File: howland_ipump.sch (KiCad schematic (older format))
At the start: 13 parts, among them Q1 BC856, U11 OPA991S

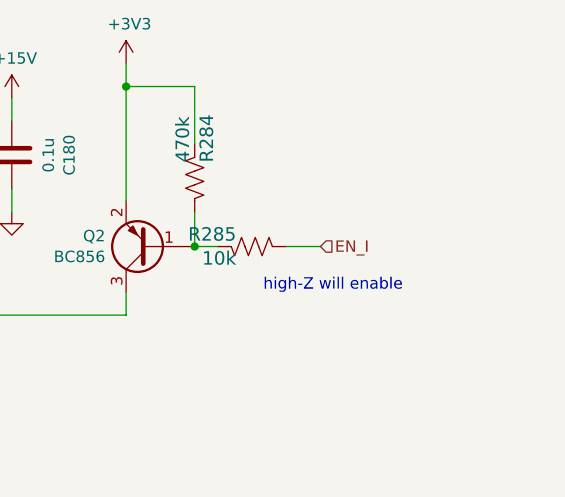
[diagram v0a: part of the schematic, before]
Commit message: layout cleanup; removed custom footrpints
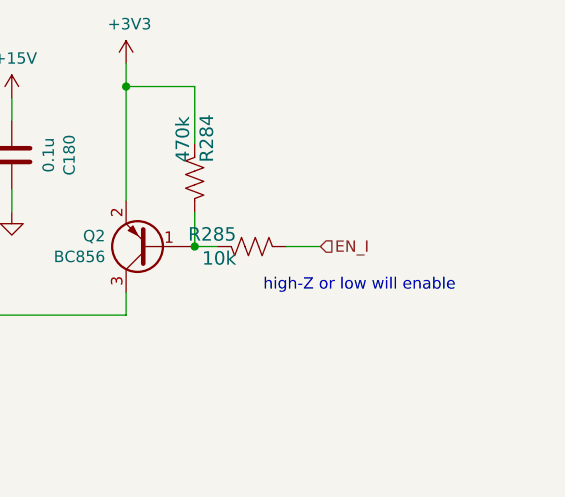
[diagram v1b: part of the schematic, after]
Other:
- note added: "high-Z or low will enable"
- note removed: "high-Z will enable"
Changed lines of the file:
@@
 EN_I
 Text Notes 8250 4250 0    50   ~ 0
-high-Z will enable
+high-Z or low will enable
 Wire Wire Line
 	5100 4000 5100 4050

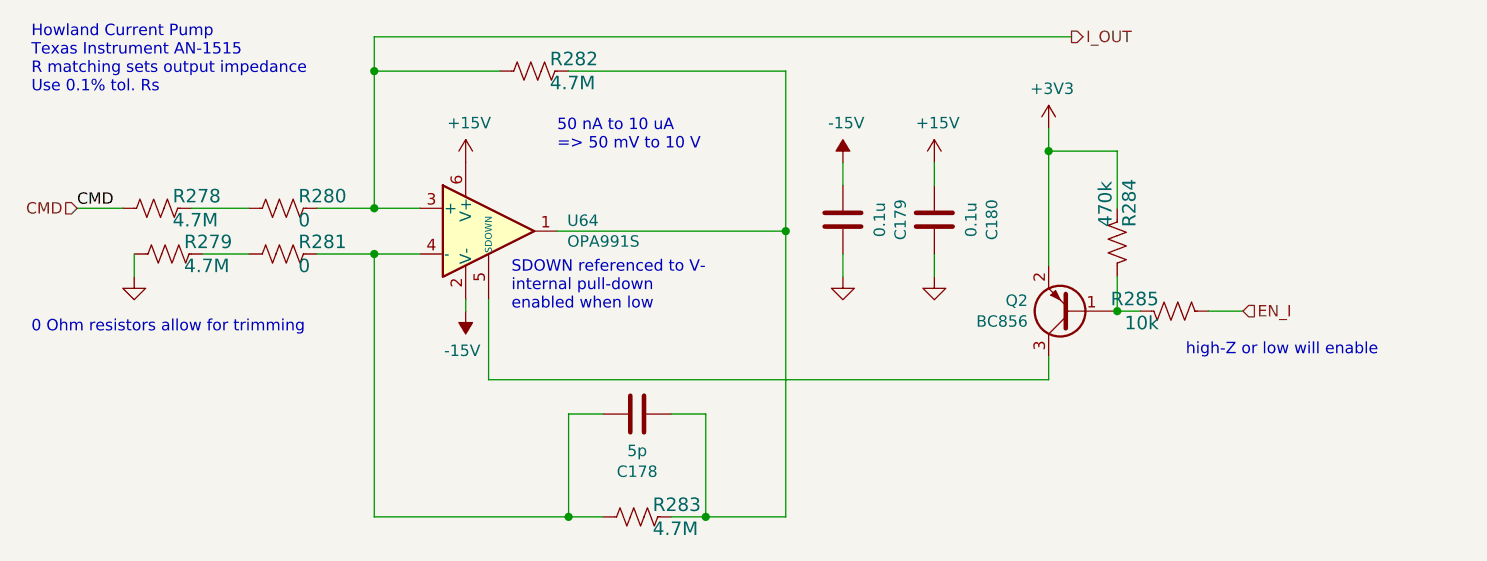
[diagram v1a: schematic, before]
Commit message: updates of DAC part placement
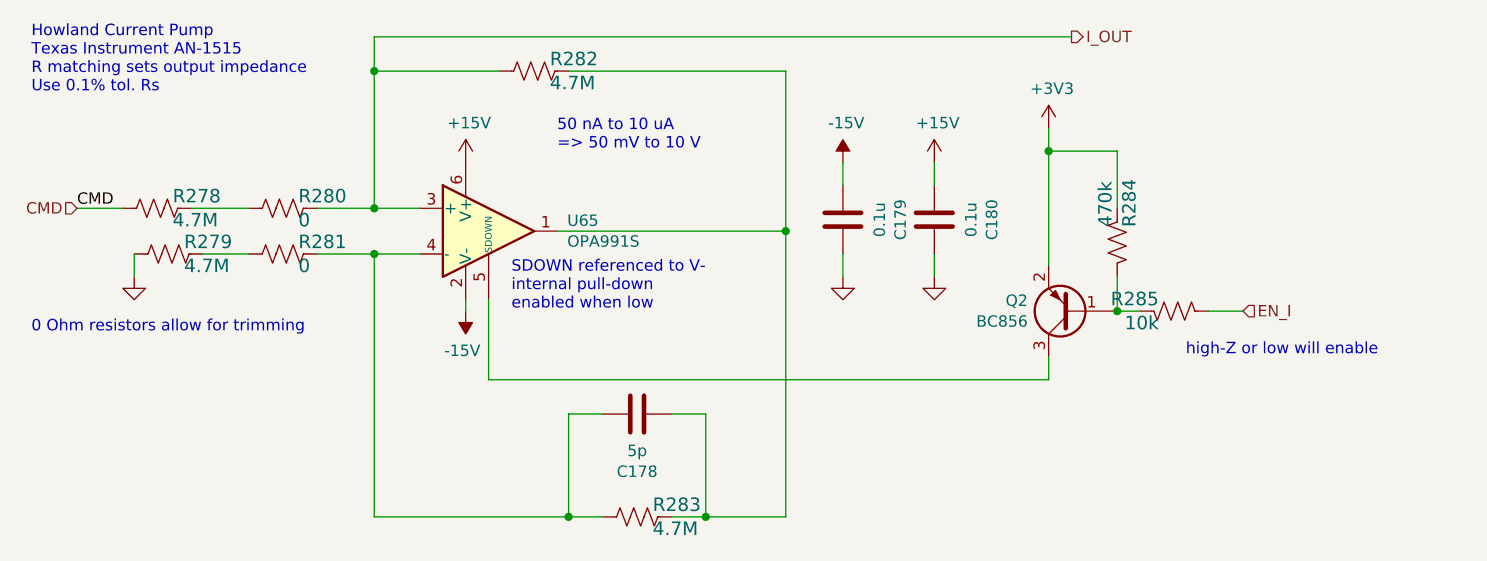
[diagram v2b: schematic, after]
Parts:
- renumbered C33 to C11, C34 to C12, C35 to C13, R28 to R27, R52 to R28, R53 to R29, R54 to R30, R59 to R31, R60 to R32, R26 to R33, R27 to R34, U11 to U12

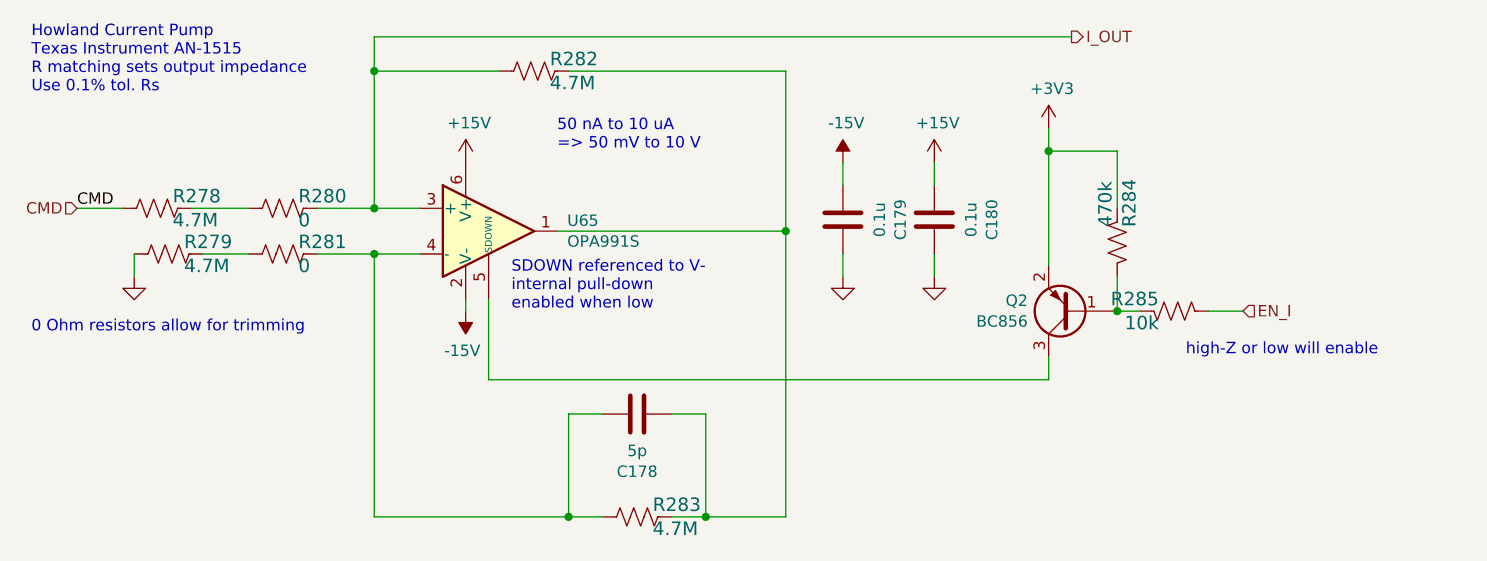
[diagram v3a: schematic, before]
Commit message: updated component placement
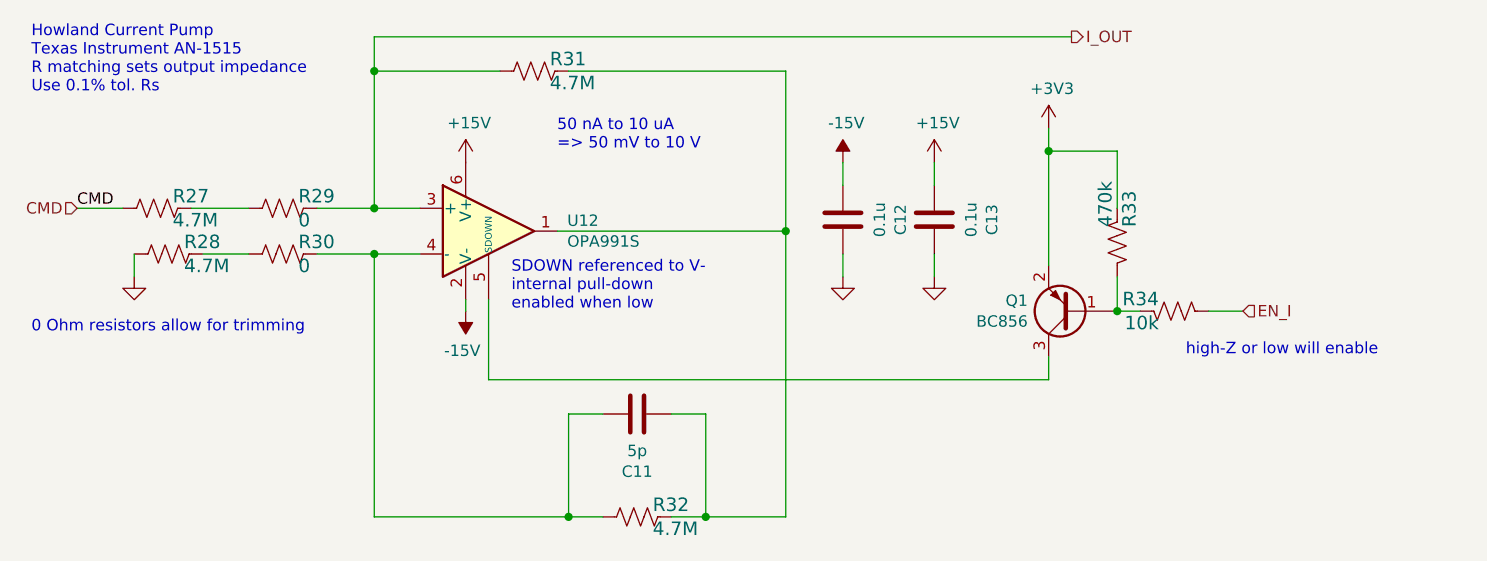
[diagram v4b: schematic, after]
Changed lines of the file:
@@
 AR Path="/6095BD4C/60C5A41E/60D781E3" Ref="#PWR?"  Part="1"
 AR Path="/61B02572/60BE01FC/60D781E3" Ref="#PWR0254"  Part="1"
-F 0 "#PWR0254" H 5100 4150 50  0001 C CNN
+F 0 "#PWR059" H 5100 4150 50  0001 C CNN
 F 1 "-15V" H 5115 4223 50  0000 C CNN
 F 2 "" H 5100 4050 50  0001 C CNN
@@
 AR Path="/6095BD4C/60C5A41E/60D781E9" Ref="#PWR?"  Part="1"
 AR Path="/61B02572/60BE01FC/60D781E9" Ref="#PWR0253"  Part="1"
-F 0 "#PWR0253" H 5100 3250 50  0001 C CNN
+F 0 "#PWR058" H 5100 3250 50  0001 C CNN
 F 1 "+15V" H 5115 3573 50  0000 C CNN
 F 2 "" H 5100 3400 50  0001 C CNN
@@
 AR Path="/6095BD4C/60C5A41E/60D781F4" Ref="C?"  Part="1"
 AR Path="/61B02572/60BE01FC/60D781F4" Ref="C178"  Part="1"
-F 0 "C178" V 5598 4500 50  0000 C CNN
+F 0 "C11" V 5598 4500 50  0000 C CNN
 F 1 "5p" V 5689 4500 50  0000 C CNN
 F 2 "Capacitor_SMD:C_0603_1608Metric" H 5888 4350 50  0001 C CNN
@@
 AR Path="/6095BD4C/60C5A41E/60D78215" Ref="#PWR?"  Part="1"
 AR Path="/61B02572/60BE01FC/60D78215" Ref="#PWR0252"  Part="1"
-F 0 "#PWR0252" H 3650 3650 50  0001 C CNN
+F 0 "#PWR057" H 3650 3650 50  0001 C CNN
 F 1 "GND" V 3655 3772 50  0001 R CNN
 F 2 "" H 3650 3900 50  0001 C CNN
@@
 AR Path="/6095BD4C/60C5A41E/60D7821F" Ref="U?"  Part="1"
 AR Path="/61B02572/60BE01FC/60D7821F" Ref="U65"  Part="1"
-F 0 "U65" H 5544 3746 50  0000 L CNN
+F 0 "U12" H 5544 3746 50  0000 L CNN
 F 1 "OPA991S" H 5544 3655 50  0000 L CNN
 F 2 "Package_TO_SOT_SMD:SOT-23-6" H 5350 3450 50  0001 L CNN
@@
 AR Path="/6095BD4C/60C5A41E/60D78240" Ref="R?"  Part="1"
 AR Path="/61B02572/60BE01FC/60D78240" Ref="R283"  Part="1"
-F 0 "R283" V 5797 5018 59  0000 L CNN
+F 0 "R32" V 5797 5018 59  0000 L CNN
 F 1 "4.7M" V 5902 5018 59  0000 L CNN
 F 2 "Resistor_SMD:R_1206_3216Metric" H 5850 4950 50  0001 C CNN
@@
 AR Path="/6095BD4C/60C5A41E/60D7824A" Ref="C?"  Part="1"
 AR Path="/61B02572/60BE01FC/60D7824A" Ref="C179"  Part="1"
-F 0 "C179" V 6498 3650 50  0000 C CNN
+F 0 "C12" V 6498 3650 50  0000 C CNN
 F 1 "0.1u" V 6589 3650 50  0000 C CNN
 F 2 "Capacitor_SMD:C_0603_1608Metric" H 6788 3500 50  0001 C CNN
@@
 AR Path="/6095BD4C/60C5A41E/60D78250" Ref="#PWR?"  Part="1"
 AR Path="/61B02572/60BE01FC/60D78250" Ref="#PWR0256"  Part="1"
-F 0 "#PWR0256" H 6750 3650 50  0001 C CNN
+F 0 "#PWR061" H 6750 3650 50  0001 C CNN
 F 1 "GND" V 6755 3772 50  0001 R CNN
 F 2 "" H 6750 3900 50  0001 C CNN
@@
 AR Path="/6095BD4C/60C5A41E/60D78256" Ref="#PWR?"  Part="1"
 AR Path="/61B02572/60BE01FC/60D78256" Ref="#PWR0257"  Part="1"
-F 0 "#PWR0257" H 7150 3250 50  0001 C CNN
+F 0 "#PWR062" H 7150 3250 50  0001 C CNN
 F 1 "+15V" H 7165 3573 50  0000 C CNN
 F 2 "" H 7150 3400 50  0001 C CNN
@@
 AR Path="/6095BD4C/60C5A41E/60D7825C" Ref="#PWR?"  Part="1"
 AR Path="/61B02572/60BE01FC/60D7825C" Ref="#PWR0258"  Part="1"
-F 0 "#PWR0258" H 7150 3650 50  0001 C CNN
+F 0 "#PWR063" H 7150 3650 50  0001 C CNN
 F 1 "GND" V 7155 3772 50  0001 R CNN
 F 2 "" H 7150 3900 50  0001 C CNN
@@
 AR Path="/6095BD4C/60C5A41E/60D78264" Ref="C?"  Part="1"
 AR Path="/61B02572/60BE01FC/60D78264" Ref="C180"  Part="1"
-F 0 "C180" V 6898 3650 50  0000 C CNN
+F 0 "C13" V 6898 3650 50  0000 C CNN
 F 1 "0.1u" V 6989 3650 50  0000 C CNN
 F 2 "Capacitor_SMD:C_0603_1608Metric" H 7188 3500 50  0001 C CNN
@@
 AR Path="/6095BD4C/60C5A41E/60D7826A" Ref="#PWR?"  Part="1"
 AR Path="/61B02572/60BE01FC/60D7826A" Ref="#PWR0255"  Part="1"
-F 0 "#PWR0255" H 6750 3500 50  0001 C CNN
+F 0 "#PWR060" H 6750 3500 50  0001 C CNN
 F 1 "-15V" H 6765 3573 50  0000 C CNN
 F 2 "" H 6750 3400 50  0001 C CNN
@@
 AR Path="/6095BD4C/60C5A41E/60D83006" Ref="R?"  Part="1"
 AR Path="/61B02572/60BE01FC/60D83006" Ref="R281"  Part="1"
-F 0 "R281" V 4247 3868 59  0000 L CNN
+F 0 "R30" V 4247 3868 59  0000 L CNN
 F 1 "0" V 4352 3868 59  0000 L CNN
 F 2 "Resistor_SMD:R_0603_1608Metric" H 4300 3800 50  0001 C CNN
@@
 AR Path="/6095BD4C/60C5A41E/60D8879F" Ref="R?"  Part="1"
 AR Path="/61B02572/60BE01FC/60D8879F" Ref="R280"  Part="1"
-F 0 "R280" V 4247 3668 59  0000 L CNN
+F 0 "R29" V 4247 3668 59  0000 L CNN
 F 1 "0" V 4352 3668 59  0000 L CNN
 F 2 "Resistor_SMD:R_0603_1608Metric" H 4300 3600 50  0001 C CNN
@@
 AR Path="/6095BD4C/60C5A41E/60B385AE" Ref="R?"  Part="1"
 AR Path="/61B02572/60BE01FC/60B385AE" Ref="R279"  Part="1"
-F 0 "R279" V 3747 3868 59  0000 L CNN
+F 0 "R28" V 3747 3868 59  0000 L CNN
 F 1 "4.7M" V 3852 3868 59  0000 L CNN
 F 2 "Resistor_SMD:R_1206_3216Metric" H 3800 3800 50  0001 C CNN
@@
 AR Path="/6095BD4C/60C5A41E/60B38EA4" Ref="R?"  Part="1"
 AR Path="/61B02572/60BE01FC/60B38EA4" Ref="R278"  Part="1"
-F 0 "R278" V 3697 3668 59  0000 L CNN
+F 0 "R27" V 3697 3668 59  0000 L CNN
 F 1 "4.7M" V 3802 3668 59  0000 L CNN
 F 2 "Resistor_SMD:R_1206_3216Metric" H 3750 3600 50  0001 C CNN
@@
 AR Path="/6095BD4C/60C5A41E/60B3940D" Ref="R?"  Part="1"
 AR Path="/61B02572/60BE01FC/60B3940D" Ref="R282"  Part="1"
-F 0 "R282" V 5347 3068 59  0000 L CNN
+F 0 "R31" V 5347 3068 59  0000 L CNN
 F 1 "4.7M" V 5452 3068 59  0000 L CNN
 F 2 "Resistor_SMD:R_1206_3216Metric" H 5400 3000 50  0001 C CNN
@@
 AR Path="/6095BD4C/60BE01FC/60BEDC00" Ref="Q1"  Part="1"
 AR Path="/61B02572/60BE01FC/60BEDC00" Ref="Q2"  Part="1"
-F 0 "Q2" H 7941 4004 50  0000 L CNN
+F 0 "Q1" H 7941 4004 50  0000 L CNN
 F 1 "BC856" H 7941 4095 50  0000 L CNN
 F 2 "Package_TO_SOT_SMD:SOT-23" H 7950 3975 50  0001 L CIN
@@
 AR Path="/6095BD4C/60C5A41E/60BF0E09" Ref="R?"  Part="1"
 AR Path="/61B02572/60BE01FC/60BF0E09" Ref="R285"  Part="1"
-F 0 "R285" V 8147 4118 59  0000 L CNN
+F 0 "R34" V 8147 4118 59  0000 L CNN
 F 1 "10k" V 8252 4118 59  0000 L CNN
 F 2 "Resistor_SMD:R_0603_1608Metric" H 8200 4050 50  0001 C CNN
@@
 AR Path="/6095BD4C/60BE01FC/60BF2F91" Ref="#PWR064"  Part="1"
 AR Path="/61B02572/60BE01FC/60BF2F91" Ref="#PWR0259"  Part="1"
-F 0 "#PWR0259" H 7650 3100 50  0001 C CNN
+F 0 "#PWR064" H 7650 3100 50  0001 C CNN
 F 1 "+3V3" H 7665 3423 50  0000 C CNN
 F 2 "" H 7650 3250 50  0001 C CNN
@@
 AR Path="/6095BD4C/60C5A41E/60C16A39" Ref="R?"  Part="1"
 AR Path="/61B02572/60BE01FC/60C16A39" Ref="R284"  Part="1"
-F 0 "R284" V 7897 3818 59  0000 L CNN
+F 0 "R33" V 7897 3818 59  0000 L CNN
 F 1 "470k" V 8002 3818 59  0000 L CNN
 F 2 "Resistor_SMD:R_0603_1608Metric" H 7950 3750 50  0001 C CNN
